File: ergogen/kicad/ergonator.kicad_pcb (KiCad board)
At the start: 2 copper layers, 122.9 x 105.2 mm, 43 parts

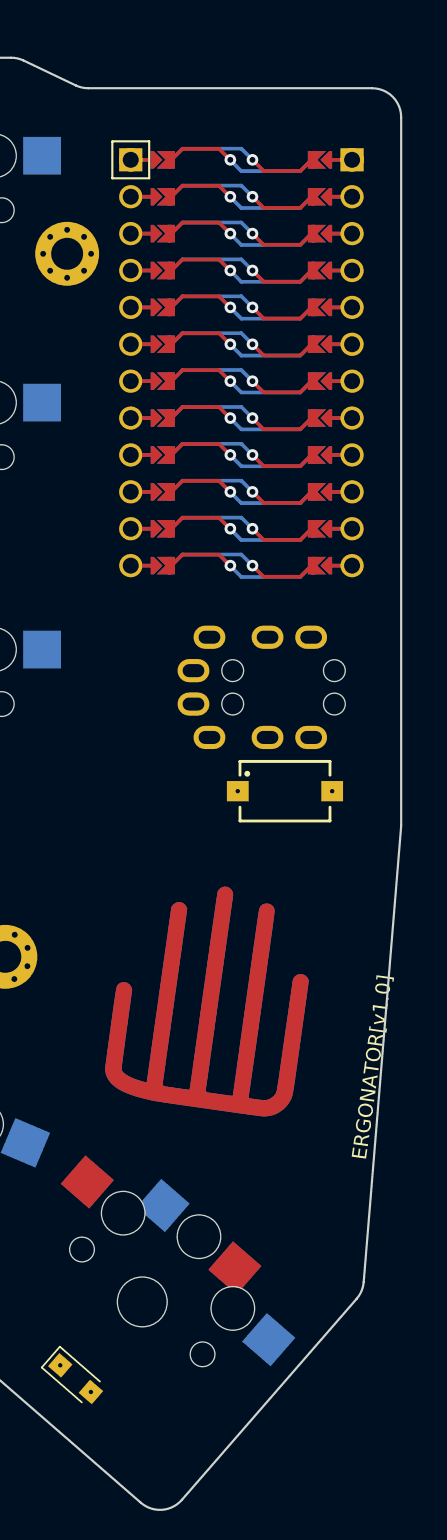
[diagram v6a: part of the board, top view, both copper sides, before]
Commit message: Changed padding variables and remade board outline.
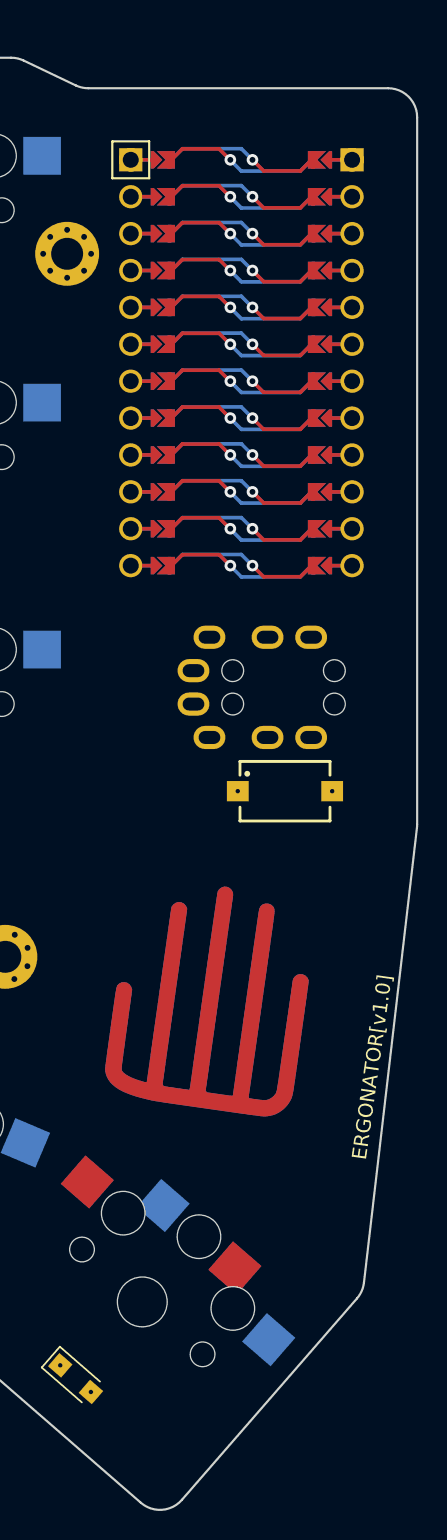
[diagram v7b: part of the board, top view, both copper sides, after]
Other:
- board size 122.9 x 105.2 mm -> 124 x 105.2 mm
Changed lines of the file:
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@@
       (pad "1" thru_hole circle locked (at 0 -1.65) (size 0.7 0.7) (drill 0.4) (layers *.Cu *.Mask))
     )
-            (gr_line (start 218.21814459116462 93.20643871179027) (end 215.64366943010108 124.52813633838377) (angle 90) (layer Edge.Cuts) (width 0.15))
-(gr_line (start 215.15981058844977 125.67641757393181) (end 203.12483774098044 139.52107014165108) (angle 90) (layer Edge.Cuts) (width 0.15))
+            (gr_line (start 219.31142889999992 93.23999367381816) (end 215.66150476207224 124.56750840946461) (angle 90) (layer Edge.Cuts) (width 0.15))
+(gr_line (start 215.18436161158573 125.64817485250592) (end 203.12483774098038 139.52107014165114) (angle 90) (layer Edge.Cuts) (width 0.15))
 (gr_line (start 200.30330044842572 139.7183713481232) (end 186.86946989999998 128.04052059999998) (angle 90) (layer Edge.Cuts) (width 0.15))
 (gr_line (start 186.86946989999998 128.04052059999998) (end 187.2676281 128.2593299) (angle 90) (layer Edge.Cuts) (width 0.15))
@@
 (gr_line (start 179.114485444 40.224657) (end 191.3720581380952 40.224657) (angle 90) (layer Edge.Cuts) (width 0.15))
 (gr_line (start 192.23351737696774 40.419694918552786) (end 195.81621562303224 42.12961908144721) (angle 90) (layer Edge.Cuts) (width 0.15))
-(gr_line (start 196.6776748619048 42.324657) (end 216.2248665 42.324657) (angle 90) (layer Edge.Cuts) (width 0.15))
-(gr_line (start 218.2248665 44.324657) (end 218.2248665 93.04260190429704) (angle 90) (layer Edge.Cuts) (width 0.15))
-(gr_arc (start 213.65039133893646 124.36429953089055) (end 215.15981053893645 125.67641753089055) (angle -36.30115384192226) (layer Edge.Cuts) (width 0.15))
-(gr_arc (start 201.61541849146704 138.20895209860979) (end 200.30330049146704 139.71837129860978) (angle -90.00000000000006) (layer Edge.Cuts) (width 0.15))
+(gr_line (start 196.6776748619048 42.324657) (end 217.32486649999998 42.324657) (angle 90) (layer Edge.Cuts) (width 0.15))
+(gr_line (start 219.32486649999998 44.324657) (end 219.32486649999998 93.00854207381803) (angle 90) (layer Edge.Cuts) (width 0.15))
+(gr_arc (start 213.67494236207224 124.33605680946448) (end 215.18436156207224 125.64817480946448) (angle -34.354508172772) (layer Edge.Cuts) (width 0.15))
+(gr_arc (start 201.61541849146698 138.20895209860984) (end 200.30330049146698 139.71837129860984) (angle -89.99999999999989) (layer Edge.Cuts) (width 0.15))
 (gr_arc (start 153.4889462621801 117.87034753191638) (end 151.5123352621801 118.17532133191638) (angle -76.22892885745983) (layer Edge.Cuts) (width 0.15))
 (gr_arc (start 145.9778805799061 95.42102535986385) (end 147.9544915799061 95.11605155986385) (angle -88.22892360192715) (layer Edge.Cuts) (width 0.15))
@@
 (gr_arc (start 191.3720581380952 42.224657) (end 192.23351733809523 40.4196949) (angle -25.513872072799884) (layer Edge.Cuts) (width 0.15))
 (gr_arc (start 196.6776748619048 40.32465700000001) (end 195.81621566190478 42.129619100000006) (angle -25.51387207280075) (layer Edge.Cuts) (width 0.15))
-(gr_arc (start 216.2248665 44.324657) (end 218.2248665 44.324657) (angle -90) (layer Edge.Cuts) (width 0.15))
-(gr_arc (start 216.2248665 93.04260190429704) (end 218.2181446 93.20643870429704) (angle -4.698844161065324) (layer Edge.Cuts) (width 0.15))
+(gr_arc (start 217.32486649999998 44.324657) (end 219.32486649999998 44.324657) (angle -90) (layer Edge.Cuts) (width 0.15))
+(gr_arc (start 217.32486649999998 93.00854207381803) (end 219.31142889999998 93.23999367381803) (angle -6.645489830216263) (layer Edge.Cuts) (width 0.15))
 (gr_line (start 105.74728500039713 96.0788046261646) (end 119.14665799702595 94.43356849870872) (angle 90) (layer Eco1.User) (width 0.15))
 (gr_line (start 120.88801172121815 92.20473759573827) (end 119.36464490257327 79.79791069802752) (angle 90) (layer Eco1.User) (width 0.15))

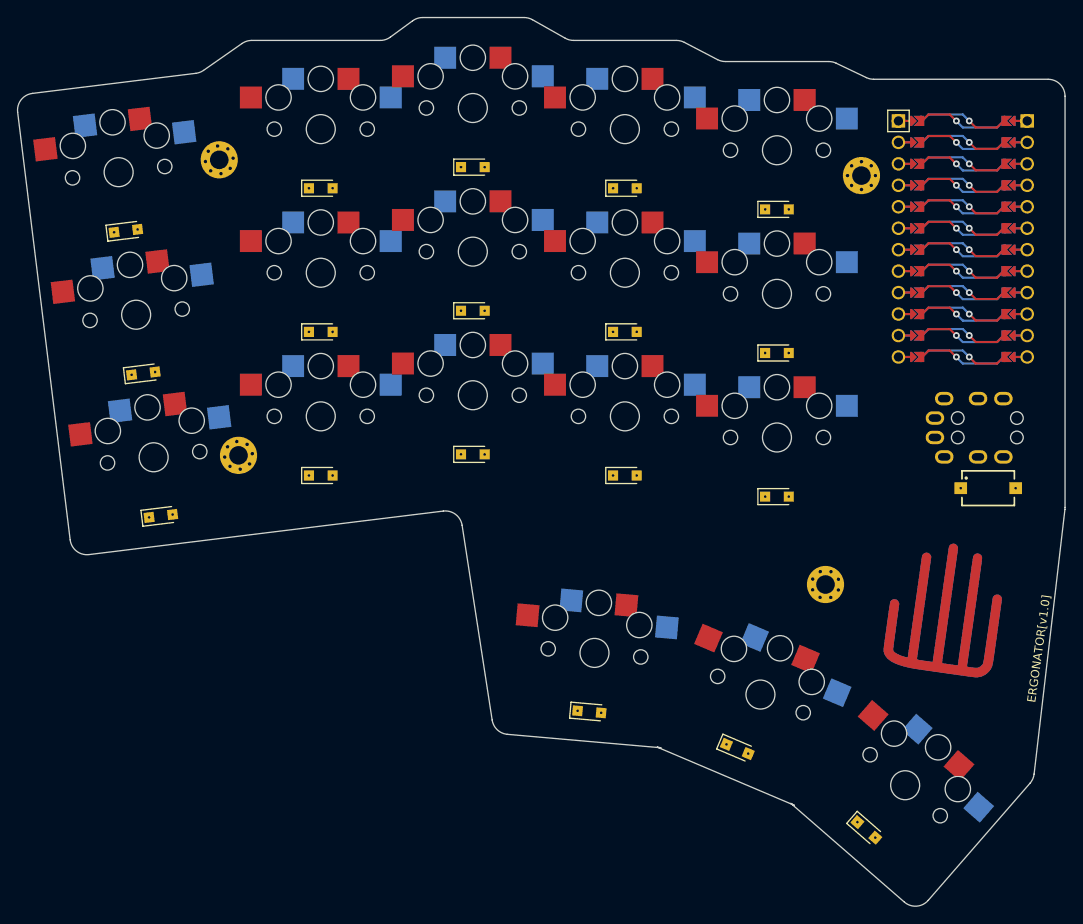
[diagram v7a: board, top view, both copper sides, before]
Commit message: Added firmware with all the layers I need so far and started on the case.
One caveat is that the config should think if the keys as mirrored for some reason and I don't know why.
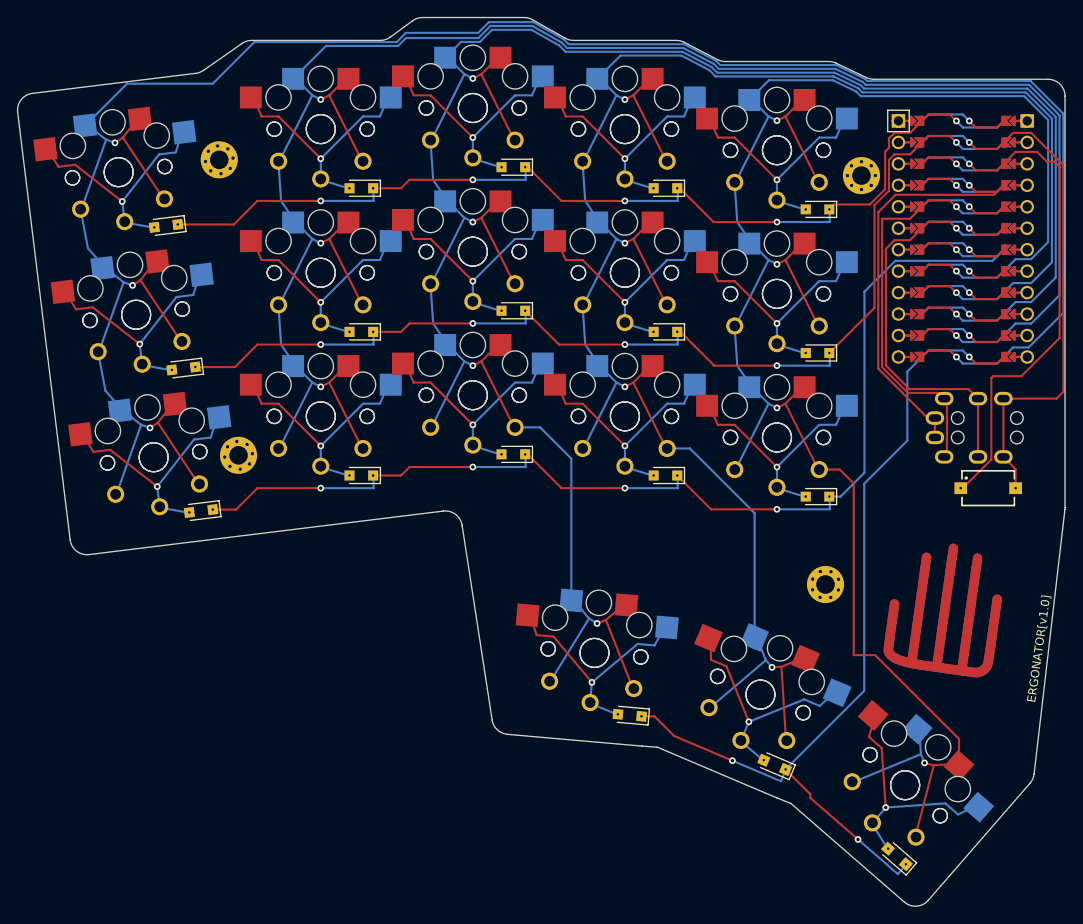
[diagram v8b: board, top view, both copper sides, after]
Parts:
- removed _10, _7, _8, _9: , MountingHole_2.2mm_M2_Pad_Via
- added S20: , PG1350, F.Cu at (109.4, 70.2)
- added S21: , PG1350, F.Cu at (107.3, 53.3)
- added S22: , PG1350, F.Cu at (131.2, 82.2)
- added S23: , PG1350, F.Cu at (131.2, 65.2)
- added S24: , PG1350, F.Cu at (131.2, 48.2)
- added S25: , PG1350, F.Cu at (149.2, 79.7)
- added S26: , PG1350, F.Cu at (149.2, 62.7)
- added S27: , PG1350, F.Cu at (149.2, 45.7)
- added S28: , PG1350, F.Cu at (167.2, 82.2)
- added S29: , PG1350, F.Cu at (167.2, 65.2)
- added S30: , PG1350, F.Cu at (167.2, 48.2)
- added S31: , PG1350, F.Cu at (185.2, 84.7)
- added S32: , PG1350, F.Cu at (185.2, 67.7)
- added S33: , PG1350, F.Cu at (185.2, 50.7)
- added S34: , PG1350, F.Cu at (163.6, 110.2)
- added S35: , PG1350, F.Cu at (183.3, 115.2)
- added S36: , PG1350, F.Cu at (200.4, 125.9)
- added S37: , 434121025816, F.Cu at (210.2, 90.7)
- added _195: , MountingHole_2.2mm_M2_Pad_Via, F.Cu at (119.2, 51.9)
- added _196: , MountingHole_2.2mm_M2_Pad_Via, F.Cu at (121.5, 86.8)
- added _197: , MountingHole_2.2mm_M2_Pad_Via, F.Cu at (195.2, 53.7)
- added _198: , MountingHole_2.2mm_M2_Pad_Via, F.Cu at (191.0, 102.1)
- D1, D10, D11, D12, D13, D14, D15, D16, D17, D18, D2, D3, D4, D5, D6, D7, D8, D9: moved to F.Cu
- S19: footprint 434121025816 -> PG1350
- moved S19 98.9 mm to (111.4, 87.1), turned to -173 degrees
- moved D11 4.80 mm to (172.0, 72.2), turned to 180 degrees
- moved D12 4.80 mm to (172.0, 55.2), turned to 180 degrees
- moved D15 4.80 mm to (190.0, 57.7), turned to 180 degrees
- moved D4 4.80 mm to (136.0, 89.2), turned to 180 degrees
- moved D5 4.80 mm to (136.0, 72.2), turned to 180 degrees
- moved D7 4.80 mm to (154.0, 86.7), turned to 180 degrees
- moved D8 4.80 mm to (154.0, 69.7), turned to 180 degrees
- moved D2 4.80 mm to (115.0, 76.6), turned to -173 degrees
- moved D13 4.80 mm to (190.0, 91.7), turned to 180 degrees
- moved D14 4.80 mm to (190.0, 74.7), turned to 180 degrees
- moved D10 4.80 mm to (172.0, 89.2), turned to 180 degrees
- moved D3 4.80 mm to (112.9, 59.7), turned to -173 degrees
- moved D17 4.80 mm to (185.0, 123.5), turned to 157 degrees
- moved D18 4.80 mm to (199.4, 134.3), turned to 139 degrees
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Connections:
- S19 pad 1: RST -> P9
- S19 pad 2: GND -> main_pinky_bottom
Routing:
- net (no net): track 262.1 -> 0.00 mm
- net P9: track 0.00 -> 260.6 mm, vias 1 -> 4
- net P7: track 0.00 -> 258.1 mm, vias 1 -> 5
- net P6: track 0.00 -> 239.1 mm, vias 1 -> 5
- net P5: track 0.00 -> 233.1 mm, vias 1 -> 5
- net P8: track 0.00 -> 230.0 mm, vias 1 -> 4
- net P4: track 0.00 -> 140.4 mm, vias 1 -> 5
- net P0: track 0.00 -> 127.6 mm, vias 1 -> 5
- net P1: track 0.00 -> 117.7 mm, vias 1 -> 5
- net P10: track 0.00 -> 106.3 mm, vias 1 -> 3
- net GND: track 0.00 -> 87.4 mm
- net RST: track 0.00 -> 63.9 mm
- net VCC: track 0.00 -> 57.0 mm
- net P2: track 0.00 -> 49.9 mm
- net P3: track 0.00 -> 49.5 mm
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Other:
- outline, holes or cut-outs redrawn
- net class Default removed
